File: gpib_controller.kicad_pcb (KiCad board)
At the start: 2 copper layers, 61.5 x 44 mm, 15 parts, among them J2 FTSH-105-01-L-DV-K, U2 SN75160BDW, U3 STM32H533RETx, Y1 MU00525-32.768K, Y2 CS10820-24M

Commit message: Update PCB
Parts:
- added J1: 112-024-113R001, Connector_Centronics:CONN_112-024-113R001_NRC, F.Cu at (215.7, 72.6)
- added J3: RJHSE5380, Connector_RJ:RJ45_Amphenol_RJHSE5380, F.Cu at (203.7, 104.3)
- added R1: 10k, Resistor_SMD:R_0603_1608Metric, F.Cu at (213.9, 124.2)
- added TP1: BOOT, TestPoint:TestPoint_Pad_D1.5mm, F.Cu at (217.7, 124.7)
- added U2: SN75160BDW, Package_SO:SOIC-20W_7.5x12.8mm_P1.27mm, F.Cu at (203.5, 122.4)
- added U4: PTS645SH43SMTR92 LFS, Button_Switch_SMD:SW_SPST_PTS645Sx43SMTR92, F.Cu at (217.5, 119.0)
- added U5: THVD1451D, Package_SO:SOIC-8_3.9x4.9mm_P1.27mm, F.Cu at (229.3, 118.4)
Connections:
- U3 pad 15: unconnected-(U3H-PA1-Pad15) -> /Overview/Microcontroller/DAV
- U3 pad 20: unconnected-(U3H-PA4-Pad20) -> /Overview/Microcontroller/NRFD
- U3 pad 26: unconnected-(U3H-PB0-Pad26) -> /Overview/Microcontroller/REN
- U3 pad 27: unconnected-(U3H-PB1-Pad27) -> /Overview/Microcontroller/EOI
- U3 pad 35: unconnected-(U3E-PB14(USART1_TX)-Pad35) -> /Overview/Microcontroller/CTRL_TX
- U3 pad 36: unconnected-(U3E-PB15(USART1_RX)-Pad36) -> /Overview/Microcontroller/CTRL_RX
- U3 pad 41: unconnected-(U3H-PA8-Pad41) -> /Overview/Microcontroller/NDAC
- U3 pad 42: unconnected-(U3H-PA9-Pad42) -> /Overview/Microcontroller/ATN
- U3 pad 43: unconnected-(U3H-PA10-Pad43) -> /Overview/Microcontroller/IFC
- U3 pad 44: unconnected-(U3C-PA11(USB_DM)-Pad44) -> /Overview/Microcontroller/REN
- U3 pad 45: unconnected-(U3C-PA12(USB_DP)-Pad45) -> /Overview/Microcontroller/EOI
- U3 pad 50: unconnected-(U3H-PA15(JTDI)-Pad50) -> /Overview/Microcontroller/SRQ
- U3 pad 60: unconnected-(U3B-BOOT0-Pad60) -> Net-(U3B-BOOT0)

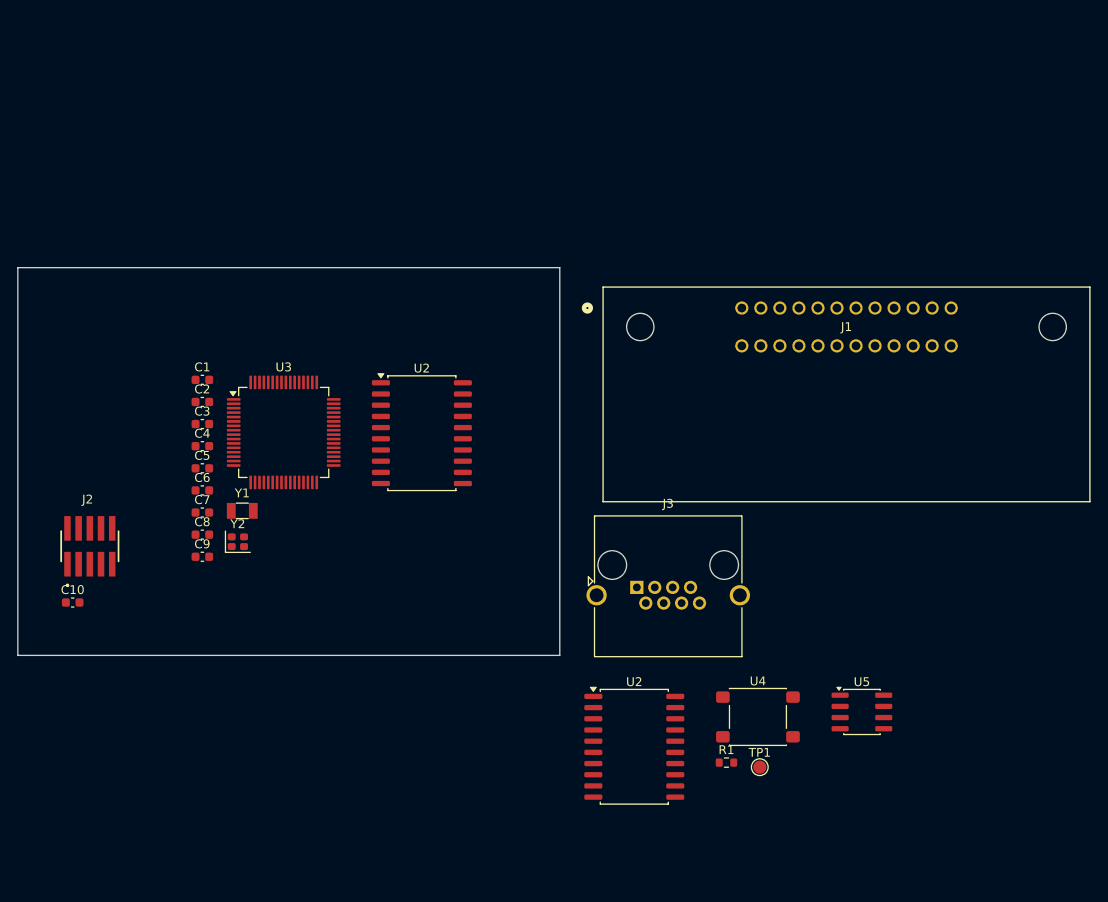
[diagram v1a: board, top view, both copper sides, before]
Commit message: Remove GPIB transcievers. Targeting modern replacements
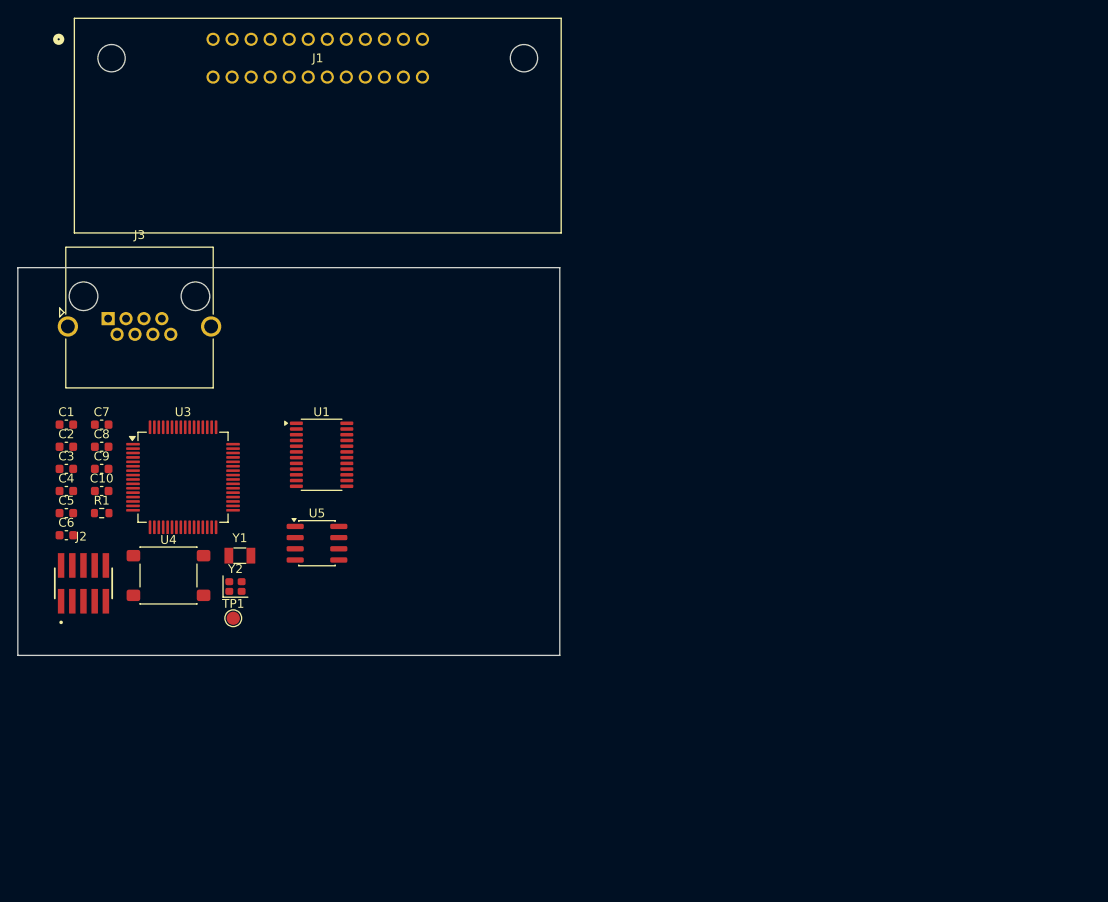
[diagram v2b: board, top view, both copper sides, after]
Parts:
- removed U2 (x2): SN75160BDW, Package_SO:SOIC-20W_7.5x12.8mm_P1.27mm
- added U1: SN74LVC8T245, Package_SO:TSSOP-24_4.4x7.8mm_P0.65mm, F.Cu at (168.0, 89.2)
- moved R1 76.3 mm to (143.0, 95.9)
- moved U4 68.8 mm to (150.6, 102.9)
- moved J1 67.3 mm to (155.7, 42.1)
- moved J3 67.3 mm to (143.7, 73.8)
- moved U5 64.7 mm to (167.4, 99.3)
- moved TP1 62.1 mm to (157.9, 107.8)
- moved C2 16.3 mm to (139.0, 88.3)
- moved C5 16.3 mm to (139.0, 95.9)
- moved C1 16.3 mm to (139.0, 85.8)
- moved C3 16.3 mm to (139.0, 90.8)
- moved C4 16.3 mm to (139.0, 93.3)
- moved C6 16.3 mm to (139.0, 98.4)
- moved C7 15.2 mm to (143.0, 85.8)
- moved C9 15.2 mm to (143.0, 90.8)
- moved C8 15.2 mm to (143.0, 88.3)
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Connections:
- net /Overview/Microcontroller/DIO5 renamed /Overview/GPIB Transceiver/iDIO5
- net /Overview/Microcontroller/DIO8 renamed /Overview/Microcontroller/iDIO8
- U3 pad 10: /Overview/Microcontroller/DIO3 -> /Overview/GPIB Transceiver/iDIO3
- U3 pad 11: /Overview/Microcontroller/DIO4 -> /Overview/GPIB Transceiver/iDIO4
- U3 pad 25: /Overview/Microcontroller/DIO6 -> /Overview/GPIB Transceiver/iDIO6
- U3 pad 37: /Overview/Microcontroller/DIO7 -> /Overview/GPIB Transceiver/iDIO7
- U3 pad 8: /Overview/Microcontroller/DIO1 -> /Overview/GPIB Transceiver/iDIO1
- U3 pad 9: /Overview/Microcontroller/DIO2 -> /Overview/GPIB Transceiver/iDIO2

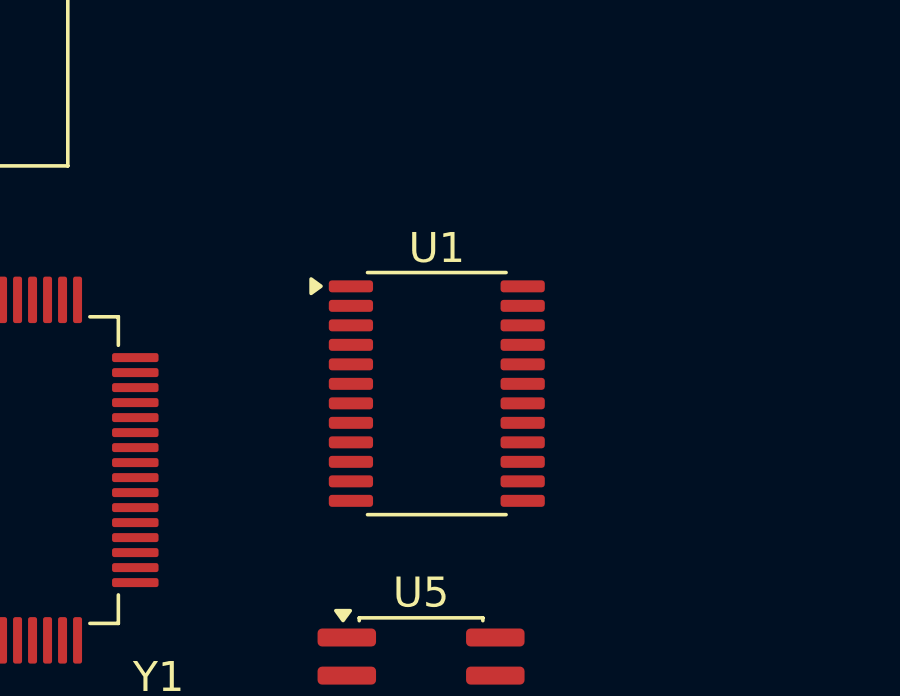
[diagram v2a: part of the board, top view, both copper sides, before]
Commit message: Changed DIO transciever to TSSOP-24
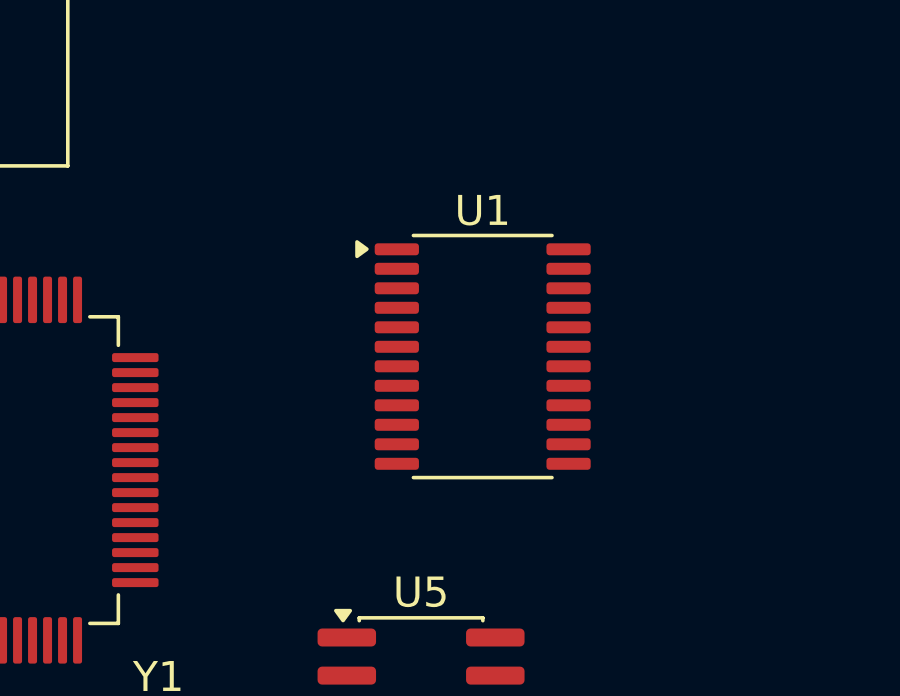
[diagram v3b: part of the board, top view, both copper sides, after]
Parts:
- U1: value SN74LVC8T245 -> SN74LVC8T245PWR
- moved U1 1.97 mm to (169.5, 88.0)

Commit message: Link DIO nets to GPIB connector
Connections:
- J1 pad 1: unconnected-(J1-Pin_1-Pad1) -> /Overview/Connectors/DIO1
- J1 pad 14: unconnected-(J1-Pin_14-Pad14) -> /Overview/Connectors/DIO6
- J1 pad 15: unconnected-(J1-Pin_15-Pad15) -> /Overview/Connectors/DIO7
- J1 pad 16: unconnected-(J1-Pin_16-Pad16) -> /Overview/Connectors/DIO8
- J1 pad 2: unconnected-(J1-Pin_2-Pad2) -> /Overview/Connectors/DIO2
- J1 pad 3: unconnected-(J1-Pin_3-Pad3) -> /Overview/Connectors/DIO3
- J1 pad 4: unconnected-(J1-Pin_4-Pad4) -> /Overview/Connectors/DIO4
- U1 pad 14: unconnected-(U1-B8-Pad14) -> /Overview/GPIB Transceiver/DIO8
- U1 pad 15: unconnected-(U1-B7-Pad15) -> /Overview/Connectors/DIO7
- U1 pad 16: unconnected-(U1-B6-Pad16) -> /Overview/Connectors/DIO6
- U1 pad 18: unconnected-(U1-B4-Pad18) -> /Overview/Connectors/DIO4
- U1 pad 19: unconnected-(U1-B3-Pad19) -> /Overview/Connectors/DIO3
- U1 pad 20: unconnected-(U1-B2-Pad20) -> /Overview/Connectors/DIO2
- U1 pad 21: unconnected-(U1-B1-Pad21) -> /Overview/Connectors/DIO1
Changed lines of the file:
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@@
 			(layers "F.Cu" "F.Mask" "F.Paste")
 			(roundrect_rratio 0.25)
-			(net "unconnected-(U1-B8-Pad14)")
+			(net "/Overview/GPIB Transceiver/DIO8")
 			(pinfunction "B8_14")
 			(pintype "bidirectional")
@@
 			(layers "F.Cu" "F.Mask" "F.Paste")
 			(roundrect_rratio 0.25)
-			(net "unconnected-(U1-B7-Pad15)")
+			(net "/Overview/Connectors/DIO7")
 			(pinfunction "B7_15")
 			(pintype "bidirectional")
@@
 			(layers "F.Cu" "F.Mask" "F.Paste")
 			(roundrect_rratio 0.25)
-			(net "unconnected-(U1-B6-Pad16)")
+			(net "/Overview/Connectors/DIO6")
 			(pinfunction "B6_16")
 			(pintype "bidirectional")
@@
 			(layers "F.Cu" "F.Mask" "F.Paste")
 			(roundrect_rratio 0.25)
-			(net "unconnected-(U1-B4-Pad18)")
+			(net "/Overview/Connectors/DIO4")
 			(pinfunction "B4_18")
 			(pintype "bidirectional")
@@
 			(layers "F.Cu" "F.Mask" "F.Paste")
 			(roundrect_rratio 0.25)
-			(net "unconnected-(U1-B3-Pad19)")
+			(net "/Overview/Connectors/DIO3")
 			(pinfunction "B3_19")
 			(pintype "bidirectional")
@@
 			(layers "F.Cu" "F.Mask" "F.Paste")
 			(roundrect_rratio 0.25)
-			(net "unconnected-(U1-B2-Pad20)")
+			(net "/Overview/Connectors/DIO2")
 			(pinfunction "B2_20")
 			(pintype "bidirectional")
@@
 			(layers "F.Cu" "F.Mask" "F.Paste")
 			(roundrect_rratio 0.25)
-			(net "unconnected-(U1-B1-Pad21)")
+			(net "/Overview/Connectors/DIO1")
 			(pinfunction "B1_21")
 			(pintype "bidirectional")
@@
 			(layers "*.Cu" "*.Mask")
 			(remove_unused_layers no)
-			(net "unconnected-(J1-Pin_1-Pad1)")
+			(net "/Overview/Connectors/DIO1")
 			(pinfunction "Pin_1_1")
 			(pintype "passive")
@@
 			(layers "*.Cu" "*.Mask")
 			(remove_unused_layers no)
-			(net "unconnected-(J1-Pin_2-Pad2)")
+			(net "/Overview/Connectors/DIO2")
 			(pinfunction "Pin_2_2")
 			(pintype "passive")
@@
 			(layers "*.Cu" "*.Mask")
 			(remove_unused_layers no)
-			(net "unconnected-(J1-Pin_3-Pad3)")
+			(net "/Overview/Connectors/DIO3")
 			(pinfunction "Pin_3_3")
 			(pintype "passive")
@@
 			(layers "*.Cu" "*.Mask")
 			(remove_unused_layers no)
-			(net "unconnected-(J1-Pin_4-Pad4)")
+			(net "/Overview/Connectors/DIO4")
 			(pinfunction "Pin_4_4")
 			(pintype "passive")
@@
 			(layers "*.Cu" "*.Mask")
 			(remove_unused_layers no)
-			(net "unconnected-(J1-Pin_14-Pad14)")
+			(net "/Overview/Connectors/DIO6")
 			(pinfunction "Pin_14_14")
 			(pintype "passive")
@@
 			(layers "*.Cu" "*.Mask")
 			(remove_unused_layers no)
-			(net "unconnected-(J1-Pin_15-Pad15)")
+			(net "/Overview/Connectors/DIO7")
 			(pinfunction "Pin_15_15")
 			(pintype "passive")
@@
 			(layers "*.Cu" "*.Mask")
 			(remove_unused_layers no)
-			(net "unconnected-(J1-Pin_16-Pad16)")
+			(net "/Overview/Connectors/DIO8")
 			(pinfunction "Pin_16_16")
 			(pintype "passive")

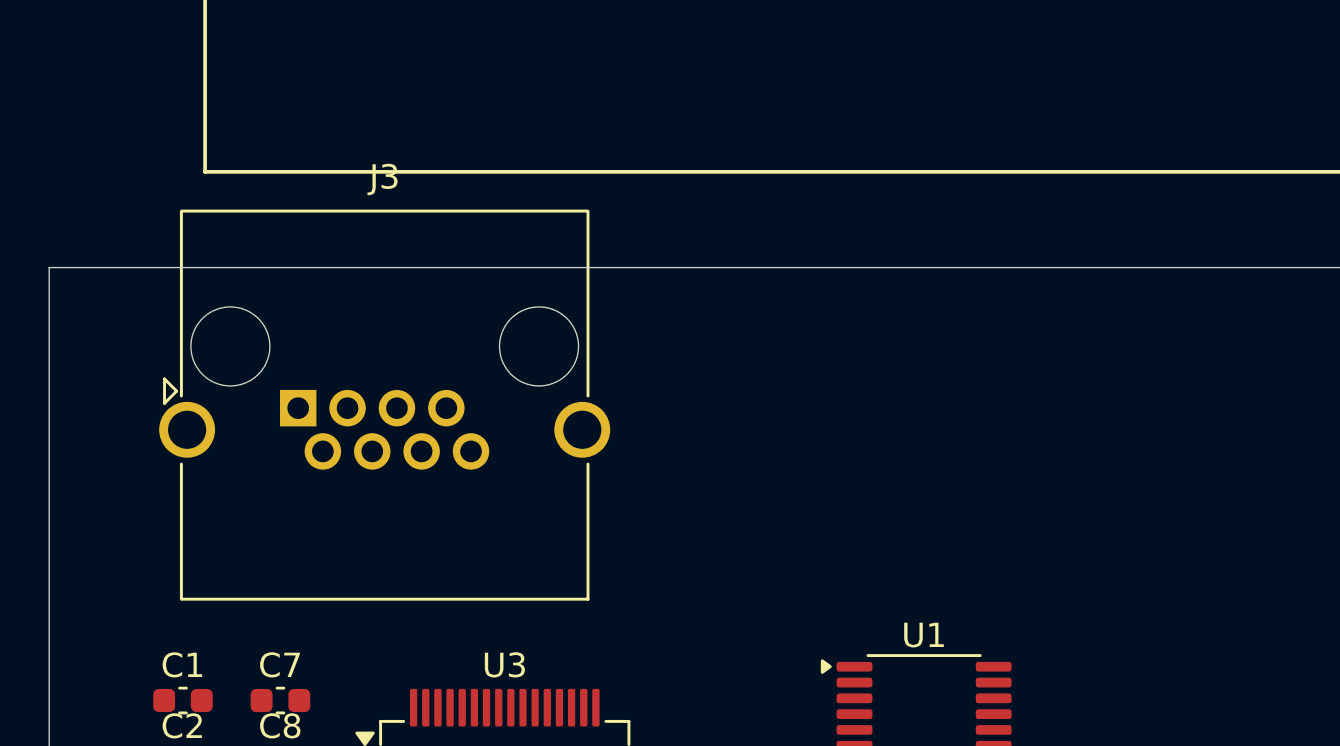
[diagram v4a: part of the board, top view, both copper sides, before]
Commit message: Added open-drain driver for GPIB control pins
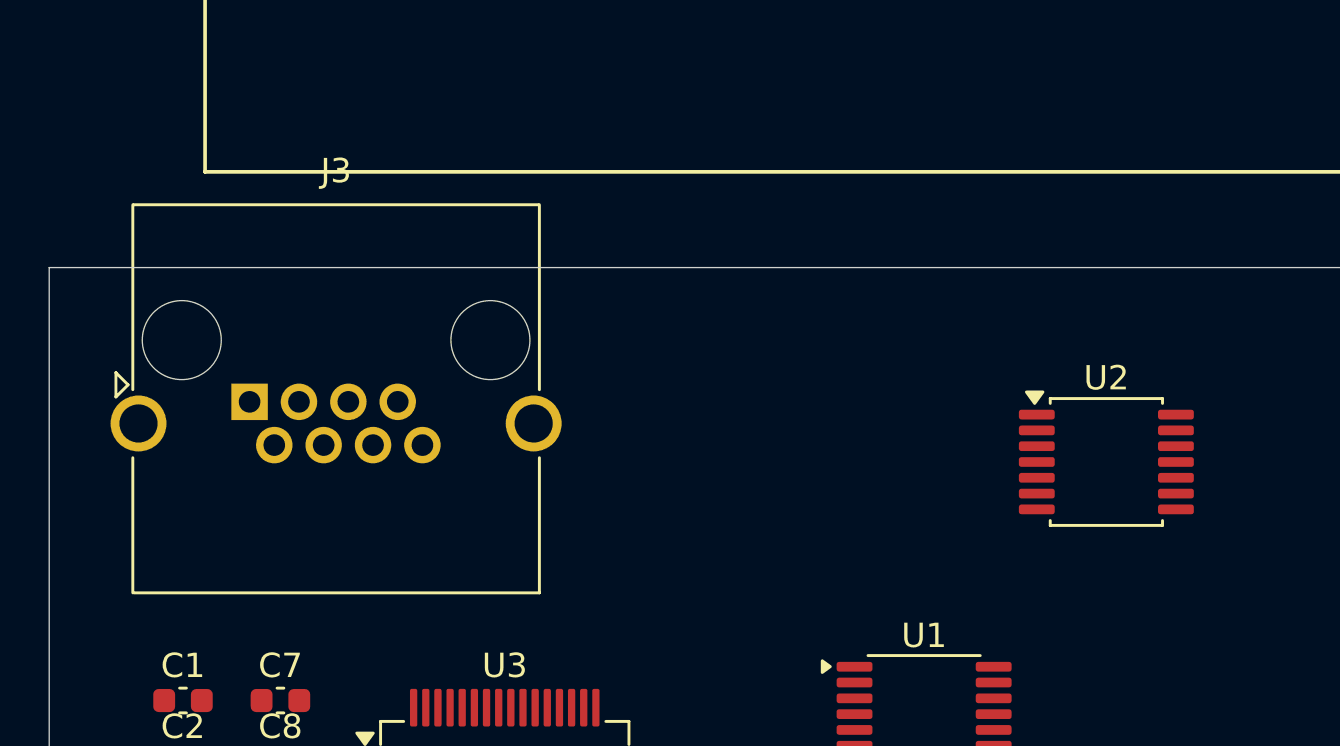
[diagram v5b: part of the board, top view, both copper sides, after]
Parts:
- added U2: SN74LVC07APWR, Package_SO:TSSOP-14_4.4x5mm_P0.65mm, F.Cu at (177.0, 76.0)
- moved J3 2.02 mm to (141.7, 73.5)
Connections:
- U3 pad 15: /Overview/Microcontroller/DAV -> /Overview/GPIB Transceiver/iDAV
- U3 pad 20: /Overview/Microcontroller/NRFD -> /Overview/GPIB Transceiver/iNRFD
- U3 pad 21: unconnected-(U3G-PA5(SPI1_SCK)-Pad21) -> /Overview/Microcontroller/DAV_SENSE
- U3 pad 22: unconnected-(U3G-PA6(SPI1_MISO)-Pad22) -> /Overview/Microcontroller/NRFD_SENSE
- U3 pad 23: unconnected-(U3G-PA7(SPI1_MOSI)-Pad23) -> /Overview/Microcontroller/NDAC_SENSE
- U3 pad 26: /Overview/Microcontroller/REN -> /Overview/Microcontroller/iREN
- U3 pad 27: /Overview/Microcontroller/EOI -> unconnected-(U3H-PB1-Pad27)
- U3 pad 29: unconnected-(U3F-PB10(I2C2_SCL)-Pad29) -> /Overview/Microcontroller/EOI_SENSE
- U3 pad 33: unconnected-(U3F-PB12(I2C2_SDA)-Pad33) -> /Overview/Microcontroller/SRQ_SENSE
- U3 pad 41: /Overview/Microcontroller/NDAC -> /Overview/GPIB Transceiver/iNDAC
- U3 pad 42: /Overview/Microcontroller/ATN -> /Overview/GPIB Transceiver/iATN
- U3 pad 43: /Overview/Microcontroller/IFC -> /Overview/GPIB Transceiver/iIFC
- U3 pad 44: /Overview/Microcontroller/REN -> /Overview/Microcontroller/USB_DM
- U3 pad 45: /Overview/Microcontroller/EOI -> /Overview/Microcontroller/USB_DP
- U3 pad 50: /Overview/Microcontroller/SRQ -> /Overview/GPIB Transceiver/iEOI
- U5 pad 2: /Overview/RS485 Transciever/CTRL_RX -> /Overview/Microcontroller/CTRL_RX
- U5 pad 3: /Overview/RS485 Transciever/CTRL_TX -> /Overview/Microcontroller/CTRL_TX
- U5 pad 5: /Overview/RS485 Transciever/CTRL_TX_N -> /Overview/Connectors/CTRL_TX_N
- U5 pad 6: /Overview/RS485 Transciever/CTRL_TX_P -> /Overview/Connectors/CTRL_TX_P
- U5 pad 7: /Overview/RS485 Transciever/CTRL_RX_N -> /Overview/Connectors/CTRL_RX_N
- U5 pad 8: /Overview/RS485 Transciever/CTRL_RX_P -> /Overview/Connectors/CTRL_RX_P

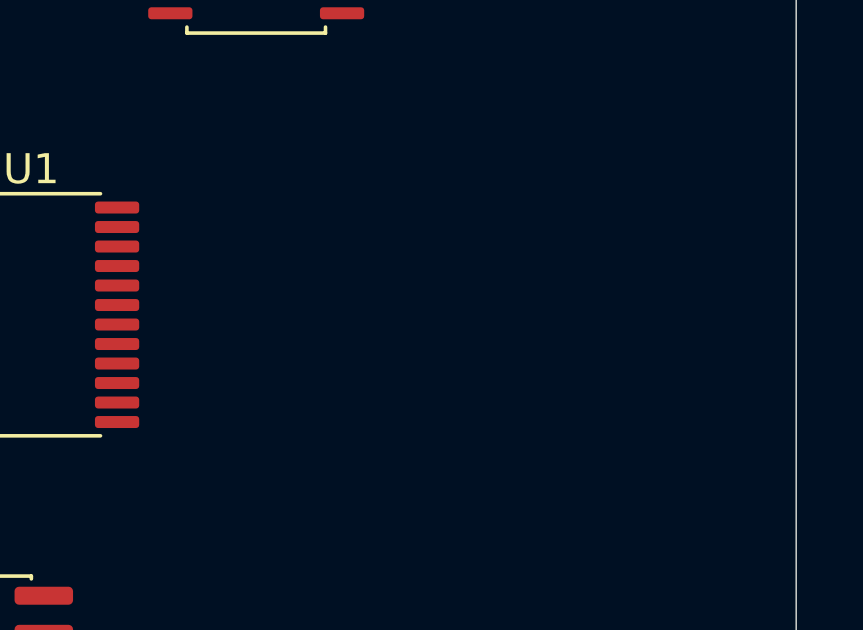
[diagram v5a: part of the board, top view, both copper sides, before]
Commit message: Add Schmitt-Trig sense IC, connect GPIB conn nets and run jobfile
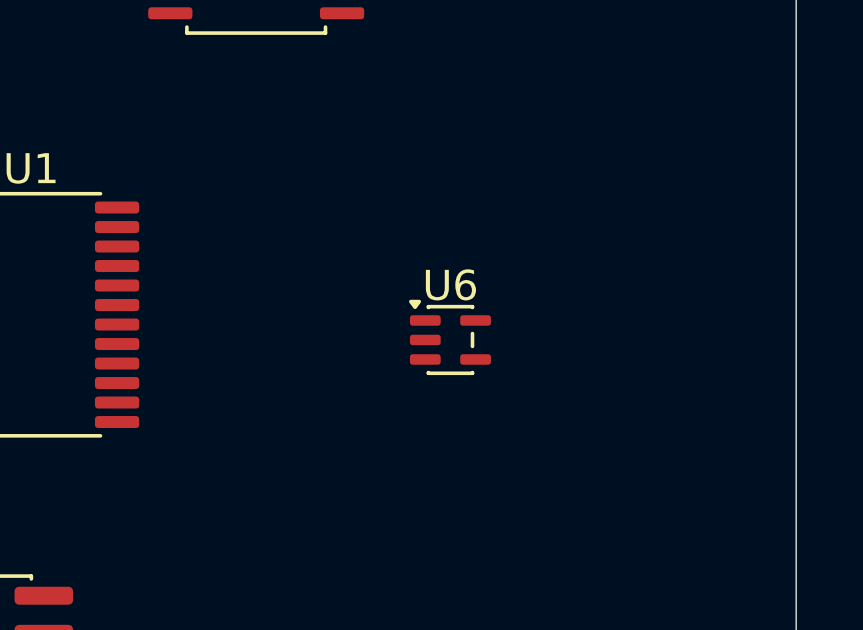
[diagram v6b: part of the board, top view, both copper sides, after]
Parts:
- added U6: SN74LVC1G07DCKR, Package_TO_SOT_SMD:SOT-353_SC-70-5, F.Cu at (183.5, 88.8)
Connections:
- U3 pad 26: /Overview/Microcontroller/iREN -> /Overview/GPIB Transceiver/iREN
